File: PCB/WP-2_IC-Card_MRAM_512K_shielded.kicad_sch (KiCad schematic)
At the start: 27 parts, among them J1 SMS-138-01-G-S, SW1 CUS-14TB, U1 MR2A08xxYSxxx, U2 MIC5317-3.3YD5, U3 4245, U4 4245, U5 4245, U6 4245

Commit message: cleanup names, cover inside corner reliefs
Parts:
- N1: footprint 000_LOCAL:WP-2_IC_Card_Cover_MRAM_512 -> 000_LOCAL:WP-2_IC-Card_Cover_MRAM_512
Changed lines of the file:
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@@
 			)
 		)
-		(property "Footprint" "000_LOCAL:WP-2_IC_Card_Cover_MRAM_512"
+		(property "Footprint" "000_LOCAL:WP-2_IC-Card_Cover_MRAM_512"
 			(at 166.37 157.48 0)
 			(effects

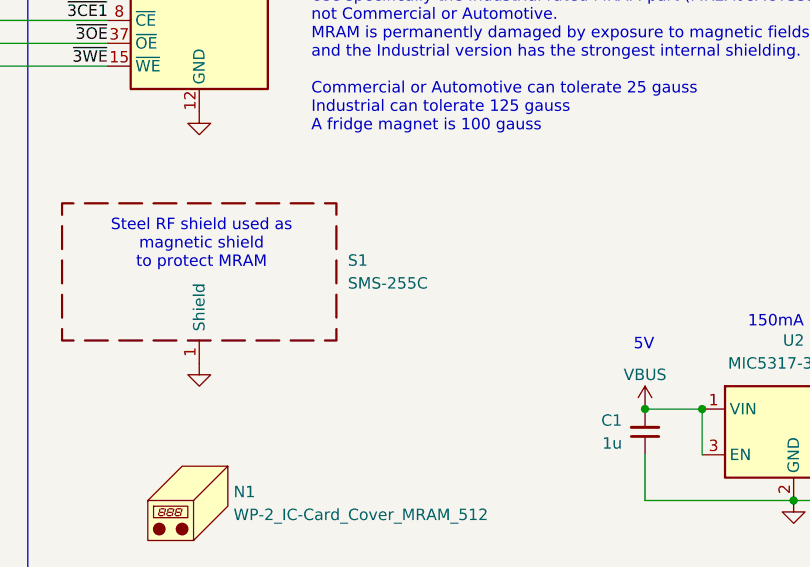
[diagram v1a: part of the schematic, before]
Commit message: better can for shielded mram
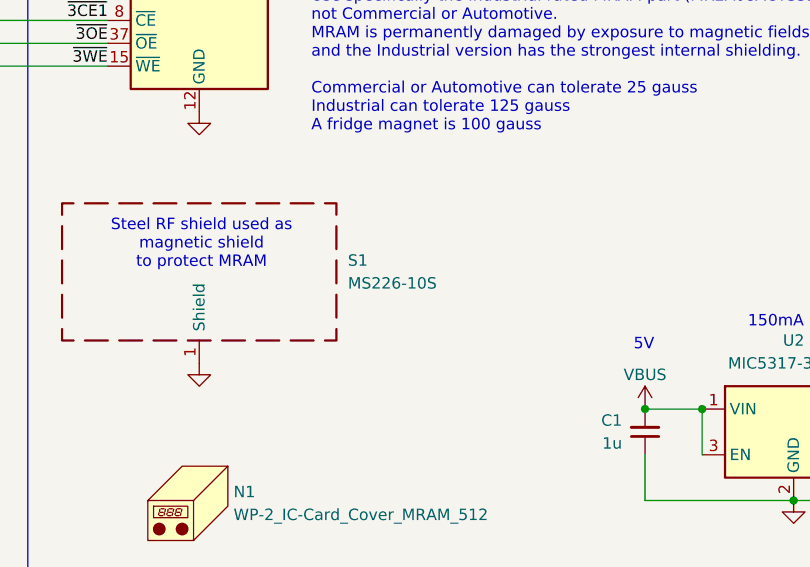
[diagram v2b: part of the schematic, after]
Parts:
- S1: value SMS-255C -> MS226-10S; footprint 000_LOCAL:SMS-255C -> 000_LOCAL:MS226-10S; MPN SMS-255C -> MS226-10S
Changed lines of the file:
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@@
 			)
 		)
-		(property "Value" "SMS-255C"
+		(property "Value" "MS226-10S"
 			(at 181.61 134.6199 0)
 			(effects
@@
 			)
 		)
-		(property "Footprint" "000_LOCAL:SMS-255C"
+		(property "Footprint" "000_LOCAL:MS226-10S"
 			(at 165.1 135.89 0)
 			(effects
@@
 			)
 		)
-		(property "Datasheet" "~"
+		(property "Datasheet" "datasheets/MS226-10.pdf"
 			(at 165.1 135.89 0)
 			(effects
@@
 			)
 		)
-		(property "MPN" "SMS-255C"
+		(property "MPN" "MS226-10S"
 			(at 165.1 133.35 0)
 			(effects

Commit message: rom wren sw, boms, footprints, shielded mram
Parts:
- C1, C10, C11, C12, C2, C3, C4, C5, C6, C7, C8, C9: footprint 000_LOCAL:C_0805_1mm -> 000_LOCAL:C_0805; MPN CL21B105KBFNFNE -> CL21A105KBCLNNC
